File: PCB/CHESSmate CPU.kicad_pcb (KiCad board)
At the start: 2 copper layers, 36 x 60.2 mm, 3 parts, among them J1 Conn_01x22_Pin, J2 Conn_01x02_Pin, U1 ESP32-DEVKITC-32D

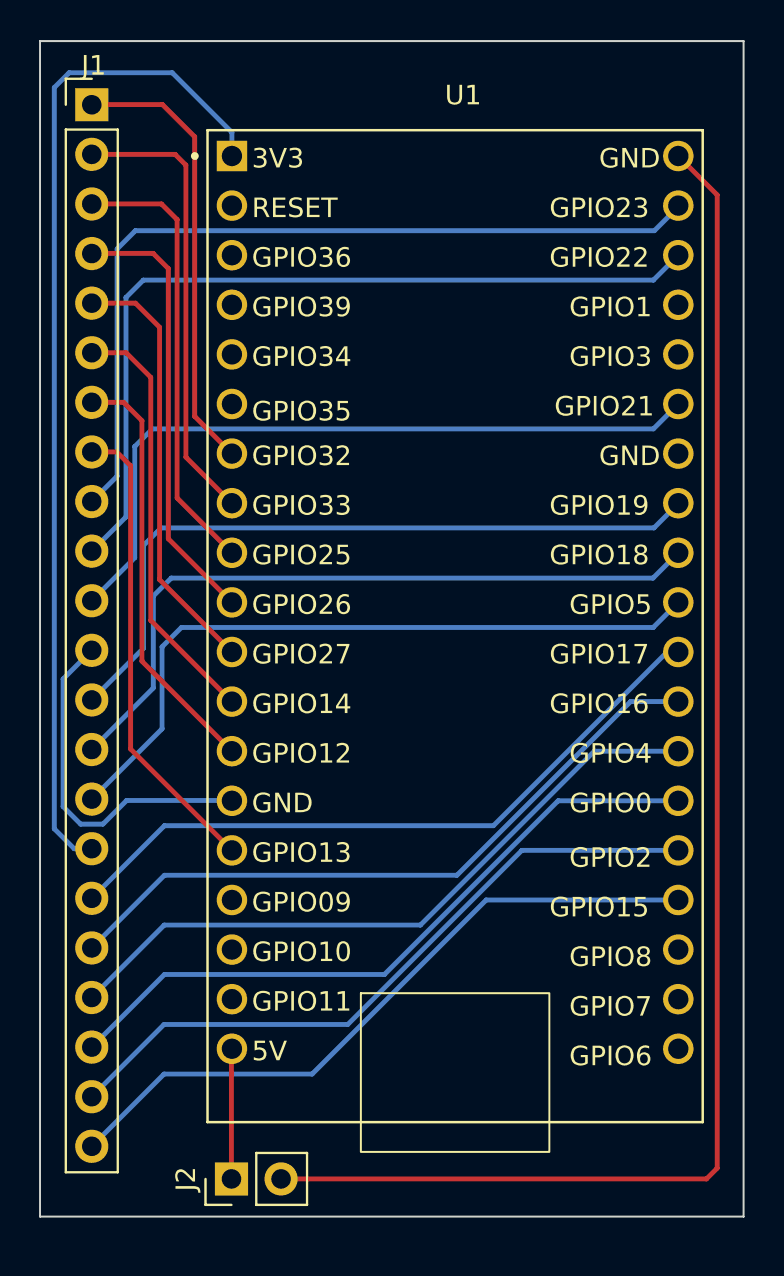
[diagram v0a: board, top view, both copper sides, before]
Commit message: 23 pin CPU connector
This doesn't work because you can't use GPIO6, so I designed a new CPU board with a Pi Pico
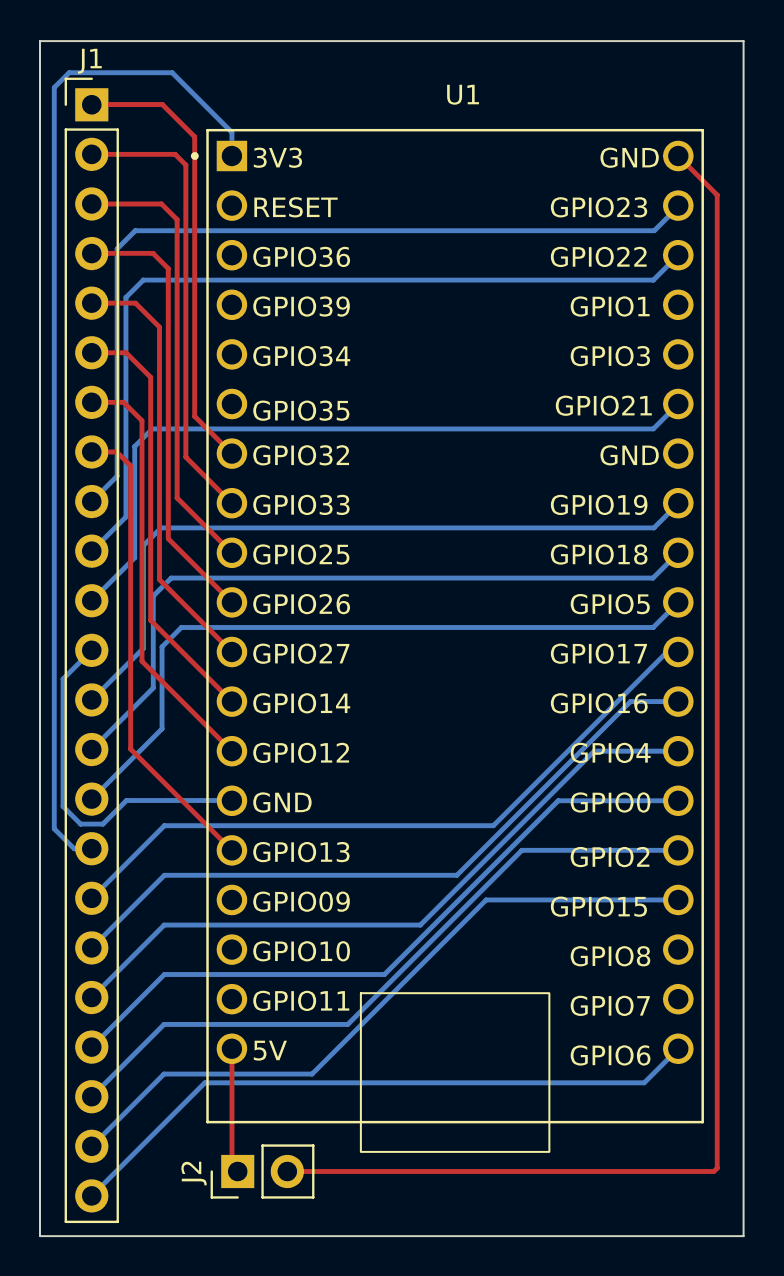
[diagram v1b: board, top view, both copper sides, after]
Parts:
- J1: value Conn_01x22_Pin -> (none); footprint Connector_PinHeader_2.54mm:PinHeader_1x22_P2.54mm_Vertical -> Connector_PinHeader_2.54mm:PinHeader_1x23_P2.54mm_Vertical
- moved J2 0.50 mm to (119.2, 112.0)
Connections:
- U1 pad J3-19: unconnected-(U1-CLK-PadJ3-19) -> Net-(J1-Pin_23)
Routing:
- net Net-(J1-Pin_23): track 0.00 -> 33.2 mm
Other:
- board size 36 x 60.2 mm -> 36 x 61.2 mm
